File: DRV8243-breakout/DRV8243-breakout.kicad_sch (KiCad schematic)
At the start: 0 parts

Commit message: Change DRV8243 to hardware varient
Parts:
- added U1: PDRV8243HRXYQ1, RXY0014A-MFG, symbol DRV8243:PDRV8243HRXYQ1
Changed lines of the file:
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@@
 	(generator_version "9.0")
 	(paper "A4")
+	(symbol
+		(lib_id "DRV8243:PDRV8243HRXYQ1")
+		(at 120.65 83.82 0)
+		(unit 1)
+		(exclude_from_sim no)
+		(in_bom yes)
+		(on_board yes)
+		(dnp no)
+		(fields_autoplaced yes)
+		(property "Reference" "U1"
+			(at 142.24 73.66 0)
+			(effects
+				(font
+					(size 1.524 1.524)
+				)
+			)
+		)
+		(property "Value" "PDRV8243HRXYQ1"
+			(at 142.24 76.2 0)
+			(effects
+				(font
+					(size 1.524 1.524)
+				)
+			)
+		)
+		(property "Footprint" "RXY0014A-MFG"
+			(at 120.65 83.82 0)
+			(effects
+				(font
+					(size 1.27 1.27)
+					(italic yes)
+				)
+				(hide yes)
+			)
+		)
+		(property "Datasheet" "PDRV8243HRXYQ1"
+			(at 120.65 83.82 0)
+			(effects
+				(font
+					(size 1.27 1.27)
+					(italic yes)
+				)
+				(hide yes)
+			)
+		)
+		(property "Description" ""
+			(at 120.65 83.82 0)
+			(effects
+				(font
+					(size 1.27 1.27)
+				)
+				(hide yes)
+			)
+		)
+		(pin "11"
+		)
+		(pin "2"
+		)
+		(pin "5"
+		)
+		(pin "1"
+		)
+		(pin "7"
+		)
+		(pin "6"
+		)
+		(pin "12"
+		)
+		(pin "14"
+		)
+		(pin "3"
+		)
+		(pin "9"
+		)
+		(pin "10"
+		)
+		(pin "8"
+		)
+		(pin "13"
+		)
+		(pin "4"
+		)
+		(instances
+			(project ""
+				(path "/72060049-abf7-41ee-aecc-769e1a200be6"
+					(reference "U1")
+					(unit 1)
+				)
+			)
+		)
+	)
 	(sheet_instances
 		(path "/"

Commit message: Minimal Setup
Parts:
- added J1: VM_Input, symbol Connector:Screw_Terminal_01x02
- added J2: Motor_Output, symbol Connector:Screw_Terminal_01x02
- added J3: MCU_Connection, symbol Connector:Conn_01x08_Pin
- added R1: 5k, symbol Device:R
- added R2: R, symbol Device:R
- added R3, R4, R5, R6: 0, symbol Device:R
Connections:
- net nFault: now reaches U1.1 (FAULT_N)
- net nFault: now also J3.6 (Pin_6), R1.2
- net IN2: now reaches U1.10 (PH_IN2)
- net IN2: now also J3.4 (Pin_4)
- net DIAG: now reaches U1.11 (DIAG)
- net DIAG: now also R4.2
- net SR: now reaches U1.12 (SR)
- net SR: now also R6.2
- net ITRIP: now reaches U1.13 (ITRIP)
- net ITRIP: now also R5.2
- net MODE: now reaches U1.14 (MODE)
- net MODE: now also R3.2
- net IPROPI: now reaches U1.2 (IPROPI)
- net IPROPI: now also J3.5 (Pin_5), R2.1
- net nSLEEP: now reaches U1.3 (SLEEP_N)
- net nSLEEP: now also J3.1 (Pin_1)
- net VM: now reaches U1.4 (VM)
- net VM: now also J1.2 (Pin_2)
- net OUT2: now reaches U1.5 (OUT2)
- net OUT2: now also J2.2 (Pin_2)
- net GND: now reaches U1.6 (GND)
- net GND: now also J1.1 (Pin_1), J3.8 (Pin_8), R2.2, R3.1, R4.1, R5.1, R6.1
- net OUT1: now reaches U1.7 (OUT1)
- net OUT1: now also J2.1 (Pin_1)
- net DRVOFF: now reaches U1.8 (DRVOFF)
- net DRVOFF: now also J3.2 (Pin_2)
- net IN1: now reaches U1.9 (EN_IN1)
- net IN1: now also J3.3 (Pin_3)
- new net Vcc: J3.7 (Pin_7), R1.1

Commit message: Power Input and protection
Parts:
- added C1: 220uF, symbol Device:C_Polarized
- added C2: 0.1uF, symbol Device:C
- added C3: DNP, symbol Device:C
- added D1: 8-10, symbol Device:D_Zener
- added Q1: PMOS, symbol Simulation_SPICE:PMOS
- added R7: 10k, symbol Device:R
- J1: value VM_Input -> Vin
- R2: value R -> 820
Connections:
- net GND: now also C1.2, C2.2, C3.2, R7.1
- net IPROPI: now also C3.1
- net VM: now also C1.1, C2.1, D1.1 (K), Q1.3 (S); no longer J1.2 (Pin_2)
- new net: J1.2 (Pin_2), Q1.1 (D)
- new net: D1.2 (A), Q1.2 (G), R7.2
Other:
- moved on the sheet: J2, J3

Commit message: footprints etc
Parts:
- added D2: LED, LED_SMD:LED_0805_2012Metric, symbol Device:LED
- added R8: 1.5k, Resistor_SMD:R_0805_2012Metric, symbol Device:R
- C1: footprint (none) -> Capacitor_SMD:CP_Elec_8x10.5
- C2, C3: footprint (none) -> Capacitor_SMD:C_0805_2012Metric
- D1: footprint (none) -> Diode_SMD:D_SOD-123
- J1, J2: footprint (none) -> TerminalBlock_Phoenix:TerminalBlock_Phoenix_MKDS-1,5-2_1x02_P5.00mm_Horizontal
- J3: footprint (none) -> Connector_PinHeader_2.54mm:PinHeader_1x08_P2.54mm_Vertical
- Q1: footprint (none) -> Package_TO_SOT_SMD:TO-252-2
- R1, R2, R3, R4, R5, R6, R7: footprint (none) -> Resistor_SMD:R_0805_2012Metric
- U1: footprint RXY0014A-MFG -> DRV8243:RXY0014A-MFG
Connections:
- net GND: now also R8.1; no longer J3.8 (Pin_8)
- net IPROPI: no longer J3.5 (Pin_5)
- net VM: now also D2.2 (A)
- net Vcc: no longer J3.7 (Pin_7)
- net nFault: no longer J3.6 (Pin_6)
- new net: D2.1 (K), R8.2
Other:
- moved on the sheet: C1, C2, C3, D1, J1, Q1, R1, R2, R3, R4, R5, R6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

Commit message: Layout
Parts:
- added H1, H2: MountingHole, MountingHole:MountingHole_3.2mm_M3, symbol Mechanical:MountingHole
- C2: footprint Capacitor_SMD:C_0805_2012Metric -> Capacitor_SMD:C_0603_1608Metric
- renumbered R7 to R1, R1 to R7
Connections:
- net DRVOFF: now also J3.4 (Pin_4); no longer J3.2 (Pin_2)
- net GND: now also J3.1 (Pin_1)
- net IN1: now also J3.5 (Pin_5); no longer J3.3 (Pin_3)
- net IN2: now also J3.6 (Pin_6); no longer J3.4 (Pin_4)
- net IPROPI: now also J3.7 (Pin_7)
- net Vcc: now also J3.2 (Pin_2)
- net nFault: now also J3.8 (Pin_8)
- net nSLEEP: now also J3.3 (Pin_3); no longer J3.1 (Pin_1)
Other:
- moved on the sheet: C3, R2, R7, U1

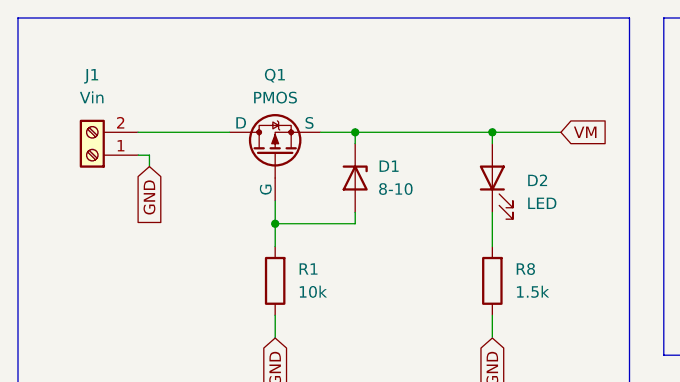
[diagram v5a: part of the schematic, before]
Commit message: Fix mosfet footprint
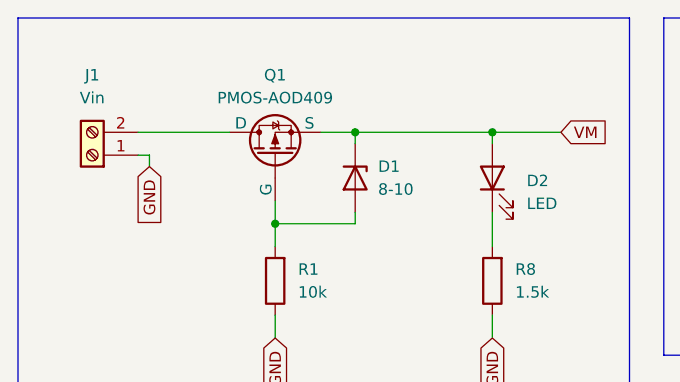
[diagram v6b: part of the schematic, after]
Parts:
- Q1: value PMOS -> PMOS-AOD409; footprint Package_TO_SOT_SMD:TO-252-2 -> DRV8243:TO-252-2(DPAK)
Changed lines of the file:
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@@
 			)
 		)
-		(property "Value" "PMOS"
+		(property "Value" "PMOS-AOD409"
 			(at 48.26 33.02 90)
 			(effects
@@
 			)
 		)
-		(property "Footprint" "Package_TO_SOT_SMD:TO-252-2"
+		(property "Footprint" "DRV8243:TO-252-2(DPAK)"
 			(at 45.72 34.29 0)
 			(effects

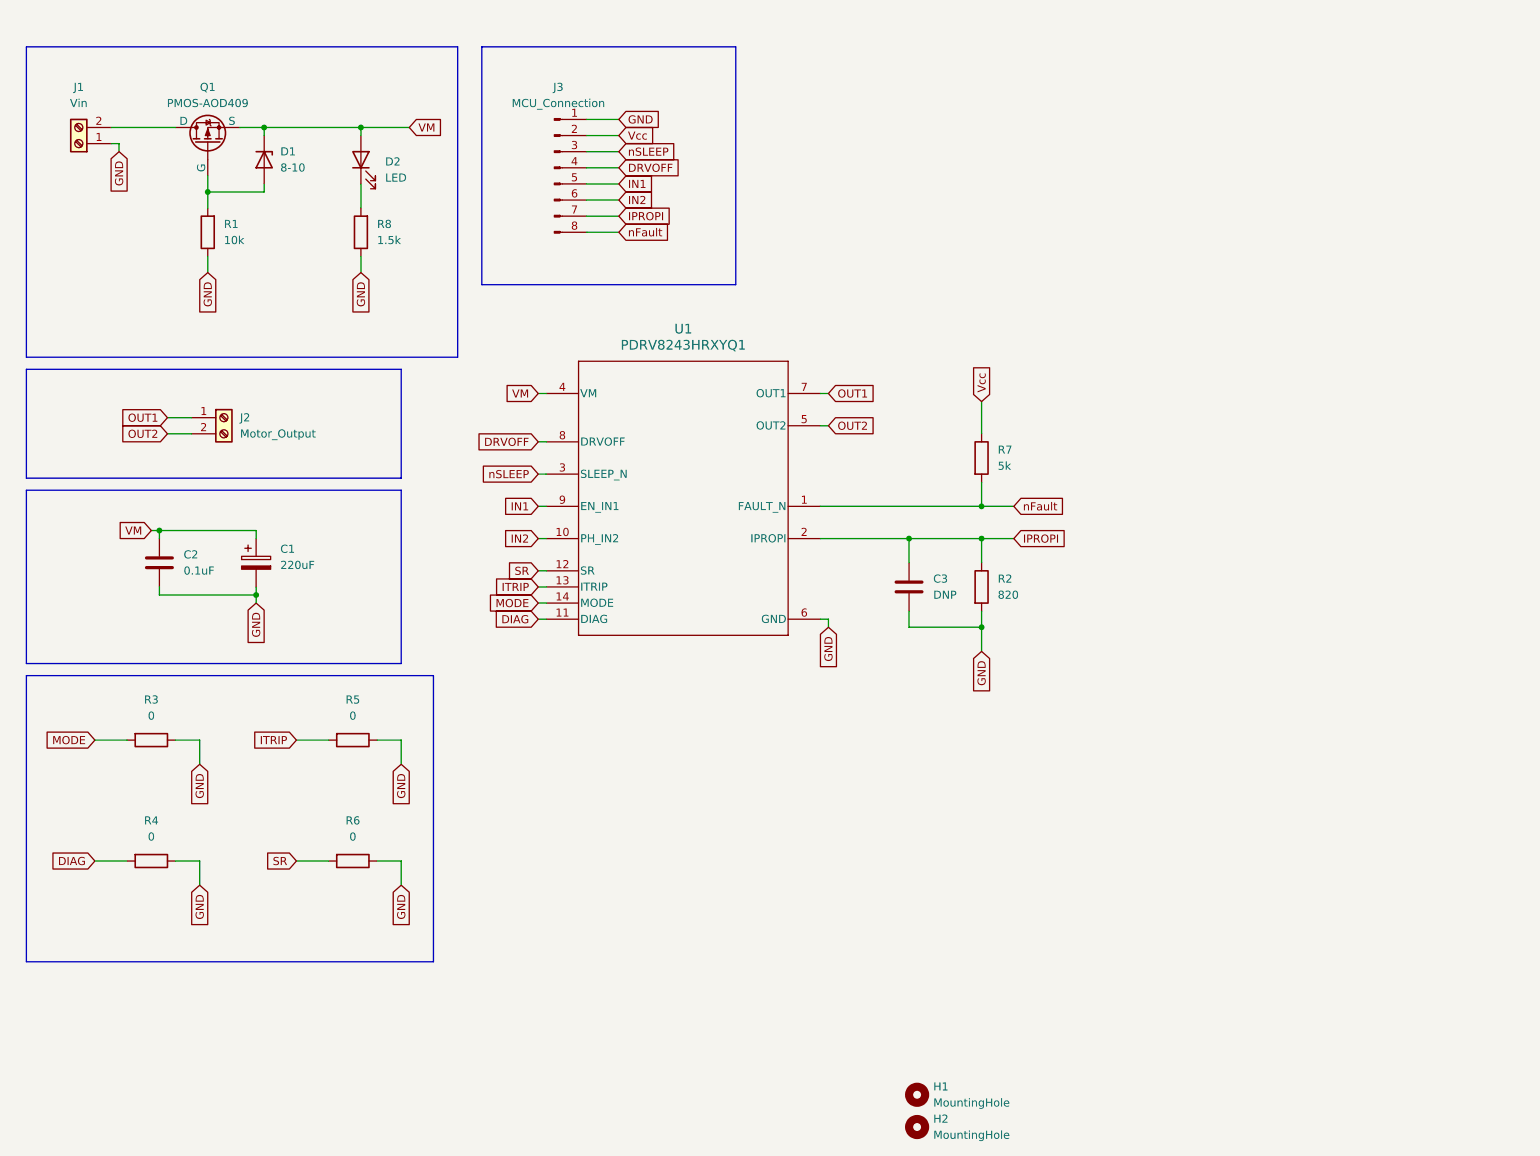
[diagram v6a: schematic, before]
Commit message: Add second driver
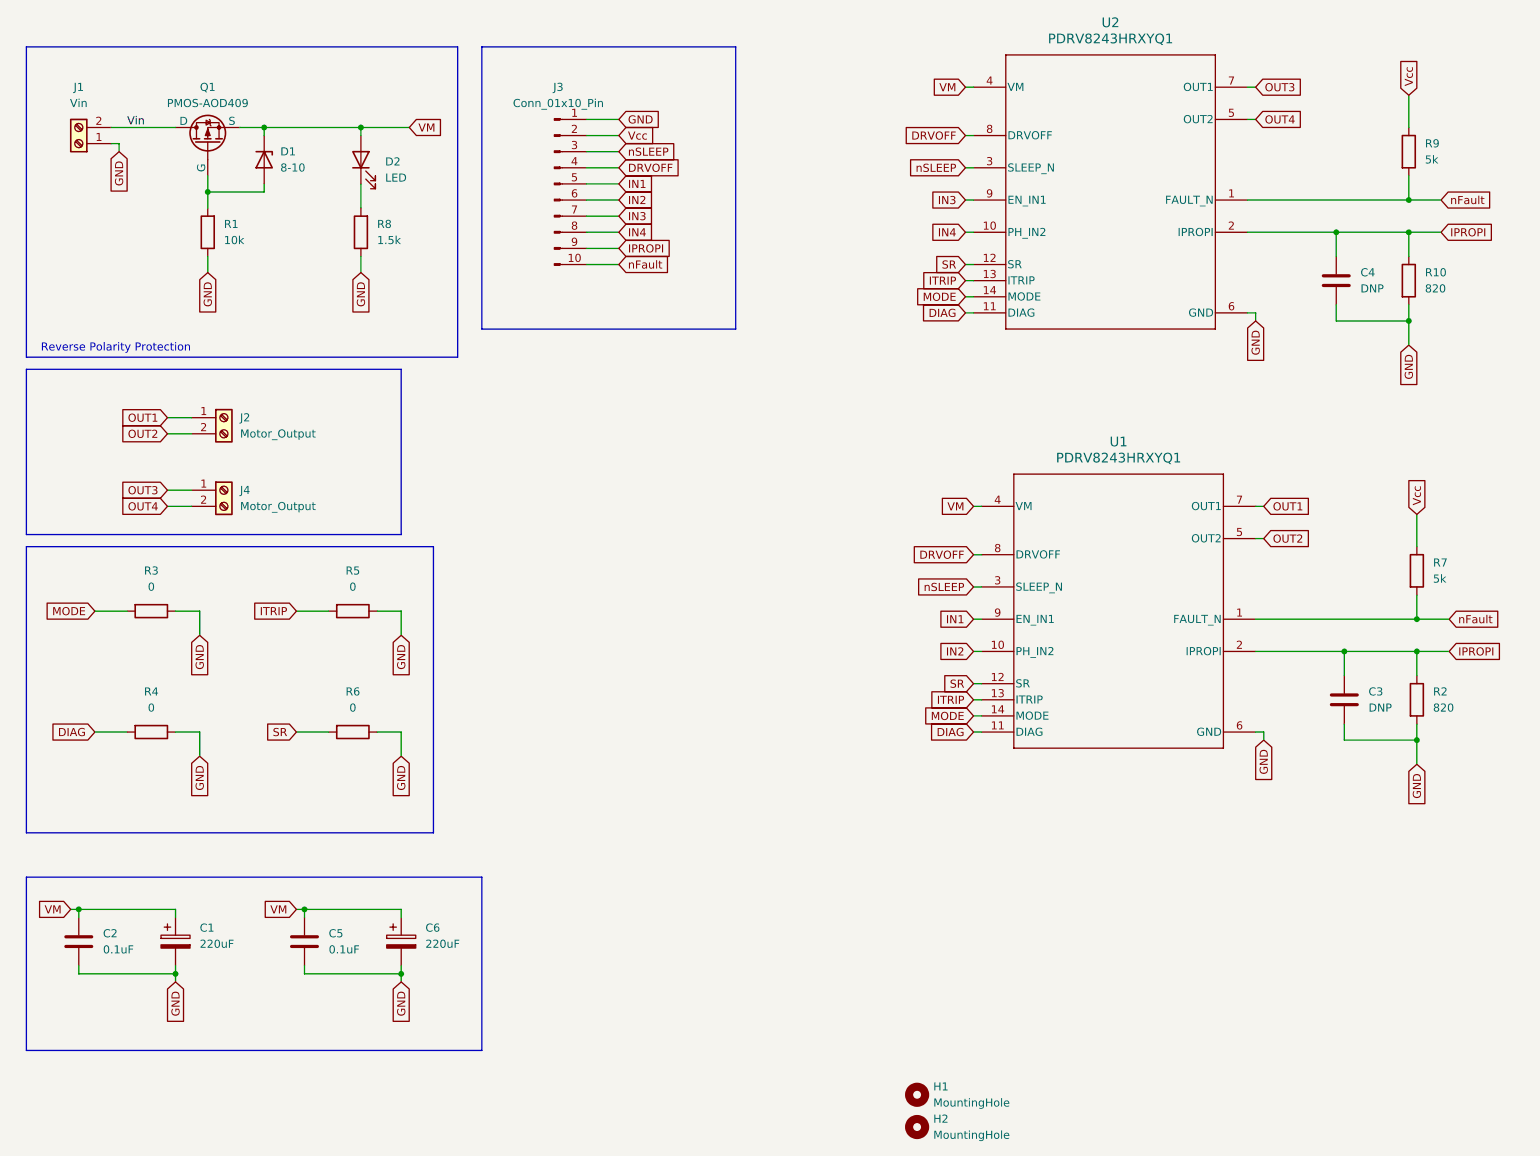
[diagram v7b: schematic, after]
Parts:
- removed J3: MCU_Connection, Connector_PinHeader_2.54mm:PinHeader_1x08_P2.54mm_Vertical, symbol Connector:Conn_01x08_Pin
- added C4: DNP, Capacitor_SMD:C_0805_2012Metric, symbol Device:C
- added C5: 0.1uF, Capacitor_SMD:C_0603_1608Metric, symbol Device:C
- added C6: 220uF, Capacitor_SMD:CP_Elec_8x10.5, symbol Device:C_Polarized
- added J3: Conn_01x10_Pin, Connector_PinHeader_2.54mm:PinHeader_1x10_P2.54mm_Vertical, symbol Connector:Conn_01x10_Pin
- added J4: Motor_Output, TerminalBlock_Phoenix:TerminalBlock_Phoenix_MKDS-1,5-2_1x02_P5.00mm_Horizontal, symbol Connector:Screw_Terminal_01x02
- added R10: 820, Resistor_SMD:R_0805_2012Metric, symbol Device:R
- added R9: 5k, Resistor_SMD:R_0805_2012Metric, symbol Device:R
- added U2: PDRV8243HRXYQ1, DRV8243:RXY0014A-MFG, symbol DRV8243:PDRV8243HRXYQ1
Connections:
- net DIAG: now also U2.11 (DIAG)
- net DRVOFF: now also J3.4 (Pin_4), U2.8 (DRVOFF)
- net GND: now also C4.2, C5.2, C6.2, J3.1 (Pin_1), R10.2, U2.6 (GND)
- net IN1: now also J3.5 (Pin_5)
- net IN2: now also J3.6 (Pin_6)
- net IPROPI: now also C4.1, J3.9 (Pin_9), R10.1, U2.2 (IPROPI)
- net ITRIP: now also U2.13 (ITRIP)
- net MODE: now also U2.14 (MODE)
- net SR: now also U2.12 (SR)
- net VM: now also C5.1, C6.1, U2.4 (VM)
- net Vcc: now also J3.2 (Pin_2), R9.1
- net nFault: now also J3.10 (Pin_10), R9.2, U2.1 (FAULT_N)
- net nSLEEP: now also J3.3 (Pin_3), U2.3 (SLEEP_N)
- net Vin: now reaches J1.2 (Pin_2), Q1.1 (D)
- new net IN3: J3.7 (Pin_7), U2.9 (EN_IN1)
- new net IN4: J3.8 (Pin_8), U2.10 (PH_IN2)
- new net OUT3: J4.1 (Pin_1), U2.7 (OUT1)
- new net OUT4: J4.2 (Pin_2), U2.5 (OUT2)
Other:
- note added: "Reverse Polarity Protection"
- moved on the sheet: C1, C2, C3, R2, R3, R4, R5, R6, R7, U1

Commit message: layout updates
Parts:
- removed J3: Conn_01x10_Pin, Connector_PinHeader_2.54mm:PinHeader_1x10_P2.54mm_Vertical, symbol Connector:Conn_01x10_Pin
- added J3: Conn_01x11_Pin, Connector_PinHeader_2.54mm:PinHeader_1x11_P2.54mm_Vertical, symbol Connector:Conn_01x11_Pin
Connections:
- net DRVOFF: now also J3.4 (Pin_4)
- net GND: now also J3.1 (Pin_1)
- net IN1: now also J3.5 (Pin_5)
- net IN2: now also J3.6 (Pin_6)
- net IN3: now also J3.7 (Pin_7)
- net IN4: now also J3.8 (Pin_8)
- net Vcc: now also J3.2 (Pin_2)
- net nFault: now also J3.11 (Pin_11)
- net nSLEEP: now also J3.3 (Pin_3)
- net IPROPI renamed IPROPI0
- net IPROPI0: now also J3.9 (Pin_9); no longer C4.1, R10.1, U2.2 (IPROPI)
- new net IPROPI1: C4.1, J3.10 (Pin_10), R10.1, U2.2 (IPROPI)
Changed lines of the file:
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@@
 	(wire
 		(pts
+			(xy 107.95 60.96) (xy 113.03 60.96)
+		)
+		(stroke
+			(width 0)
+			(type default)
+		)
+	)
+	(wire
+		(pts
 			(xy 46.99 113.03) (xy 43.18 113.03)
 		)
@@
 	(wire
 		(pts
+			(xy 107.95 58.42) (xy 113.03 58.42)
+		)
+		(stroke
+			(width 0)
+			(type default)
+		)
+	)
+	(wire
+		(pts
 			(xy 167.64 53.34) (xy 168.91 53.34)
 		)
@@
 	(wire
 		(pts
-			(xy 107.95 55.88) (xy 113.03 55.88)
-		)
-		(stroke
-			(width 0)
-			(type default)
-		)
-	)
-	(wire
-		(pts
 			(xy 34.29 39.37) (xy 34.29 40.64)
 		)
@@
 	(wire
 		(pts
-			(xy 107.95 58.42) (xy 113.03 58.42)
-		)
-		(stroke
-			(width 0)
-			(type default)
-		)
-	)
-	(wire
-		(pts
 			(xy 226.06 67.31) (xy 237.49 67.31)
 		)
@@
 	(wire
 		(pts
+			(xy 107.95 55.88) (xy 113.03 55.88)
+		)
+		(stroke
+			(width 0)
+			(type default)
+		)
+	)
+	(wire
+		(pts
 			(xy 212.09 35.56) (xy 213.36 35.56)
 		)
@@
 		)
 	)
-	(global_label "IPROPI"
+	(global_label "IPROPI0"
 		(shape input)
 		(at 113.03 55.88 0)
@@
 		)
 		(property "Intersheetrefs" "${INTERSHEET_REFS}"
-			(at 122.3653 55.88 0)
+			(at 123.5748 55.88 0)
 			(effects
 				(font
@@
 	(global_label "nFault"
 		(shape input)
-		(at 113.03 58.42 0)
+		(at 113.03 60.96 0)
 		(fields_autoplaced yes)
 		(effects
@@
 		)
 		(property "Intersheetrefs" "${INTERSHEET_REFS}"
-			(at 121.9417 58.42 0)
+			(at 121.9417 60.96 0)
 			(effects
 				(font
@@
 		)
 	)
+	(global_label "IPROPI1"
+		(shape input)
+		(at 113.03 58.42 0)
+		(fields_autoplaced yes)
+		(effects
+			(font
+				(size 1.27 1.27)
+			)
+			(justify left)
+		)
+		(property "Intersheetrefs" "${INTERSHEET_REFS}"
+			(at 123.5748 58.42 0)
+			(effects
+				(font
+					(size 1.27 1.27)
+				)
+				(justify left)
+				(hide yes)
+			)
+		)
+	)
 	(global_label "nSLEEP"
 		(shape input)
@@
 		)
 	)
-	(global_label "IPROPI"
+	(global_label "IPROPI1"
 		(shape input)
 		(at 242.57 53.34 0)
@@
 		)
 		(property "Intersheetrefs" "${INTERSHEET_REFS}"
-			(at 251.9053 53.34 0)
+			(at 253.1148 53.34 0)
 			(effects
 				(font
@@
 		)
 	)
-	(global_label "IPROPI"
+	(global_label "IPROPI0"
 		(shape input)
 		(at 243.84 119.38 0)
@@
 		)
 		(property "Intersheetrefs" "${INTERSHEET_REFS}"
-			(at 253.1753 119.38 0)
+			(at 254.3848 119.38 0)
 			(effects
 				(font
@@
 	)
 	(symbol
-		(lib_id "Device:C_Polarized")
-		(at 43.18 165.1 0)
+		(lib_id "Connector:Conn_01x11_Pin")
+		(at 102.87 48.26 0)
 		(unit 1)
 		(exclude_from_sim no)
@@
 		(dnp no)
 		(fields_autoplaced yes)
-		(property "Reference" "C1"
-			(at 46.99 162.9409 0)
+		(property "Reference" "J3"
+			(at 103.505 30.48 0)
 			(effects
 				(font
 					(size 1.27 1.27)
 				)
-				(justify left)
 			)
 		)
-		(property "Value" "220uF"
-			(at 46.99 165.4809 0)
+		(property "Value" "Conn_01x11_Pin"
+			(at 103.505 33.02 0)
 			(effects
 				(font
 					(size 1.27 1.27)
 				)
-				(justify left)
 			)
 		)
-		(property "Footprint" "Capacitor_SMD:CP_Elec_8x10.5"
-			(at 44.1452 168.91 0)
+		(property "Footprint" "Connector_PinHeader_2.54mm:PinHeader_1x11_P2.54mm_Vertical"
+			(at 102.87 48.26 0)
 			(effects
 				(font
@@
 		)
 		(property "Datasheet" "~"
-			(at 43.18 165.1 0)
+			(at 102.87 48.26 0)
 			(effects
 				(font
@@
 			)
 		)
-		(property "Description" "Polarized capacitor"
-			(at 43.18 165.1 0)
+		(property "Description" "Generic connector, single row, 01x11, script generated"
+			(at 102.87 48.26 0)
 			(effects
 				(font
@@
 			)
 		)
-		(pin "1"
+		(pin "3"
+		)
+		(pin "11"
 		)
 		(pin "2"
 		)
+		(pin "4"
+		)
+		(pin "1"
+		)
+		(pin "5"
+		)
+		(pin "6"
+		)
+		(pin "7"
+		)
+		(pin "8"
+		)
+		(pin "9"
+		)
+		(pin "10"
+		)
 		(instances
 			(project ""
 				(path "/72060049-abf7-41ee-aecc-769e1a200be6"
-					(reference "C1")
+					(reference "J3")
 					(unit 1)
 				)
@@
 	)
 	(symbol
-		(lib_id "Connector:Conn_01x10_Pin")
-		(at 102.87 45.72 0)
+		(lib_id "Device:C_Polarized")
+		(at 43.18 165.1 0)
 		(unit 1)
 		(exclude_from_sim no)
@@
 		(dnp no)
 		(fields_autoplaced yes)
-		(property "Reference" "J3"
-			(at 103.505 30.48 0)
+		(property "Reference" "C1"
+			(at 46.99 162.9409 0)
 			(effects
 				(font
 					(size 1.27 1.27)
 				)
+				(justify left)
 			)
 		)
-		(property "Value" "Conn_01x10_Pin"
-			(at 103.505 33.02 0)
+		(property "Value" "220uF"
+			(at 46.99 165.4809 0)
 			(effects
 				(font
 					(size 1.27 1.27)
 				)
+				(justify left)
 			)
 		)
-		(property "Footprint" "Connector_PinHeader_2.54mm:PinHeader_1x10_P2.54mm_Vertical"
-			(at 102.87 45.72 0)
+		(property "Footprint" "Capacitor_SMD:CP_Elec_8x10.5"
+			(at 44.1452 168.91 0)
 			(effects
 				(font
@@
 		)
 		(property "Datasheet" "~"
-			(at 102.87 45.72 0)
+			(at 43.18 165.1 0)
 			(effects
 				(font
@@
 			)
 		)
-		(property "Description" "Generic connector, single row, 01x10, script generated"
-			(at 102.87 45.72 0)
+		(property "Description" "Polarized capacitor"
+			(at 43.18 165.1 0)
 			(effects
 				(font
@@
 		(pin "1"
 		)
-		(pin "6"
-		)
 		(pin "2"
 		)
-		(pin "5"
-		)
-		(pin "3"
-		)
-		(pin "7"
-		)
-		(pin "4"
-		)
-		(pin "8"
-		)
-		(pin "9"
-		)
-		(pin "10"
-		)
 		(instances
 			(project ""
 				(path "/72060049-abf7-41ee-aecc-769e1a200be6"
-					(reference "J3")
+					(reference "C1")
 					(unit 1)
 				)
